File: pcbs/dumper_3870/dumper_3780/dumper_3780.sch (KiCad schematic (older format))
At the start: 23 parts, among them J1 Conn_01x03_Female, U1 MK3870, U2 Pico, U3 LM317T, U4 4066, U5 LM317T

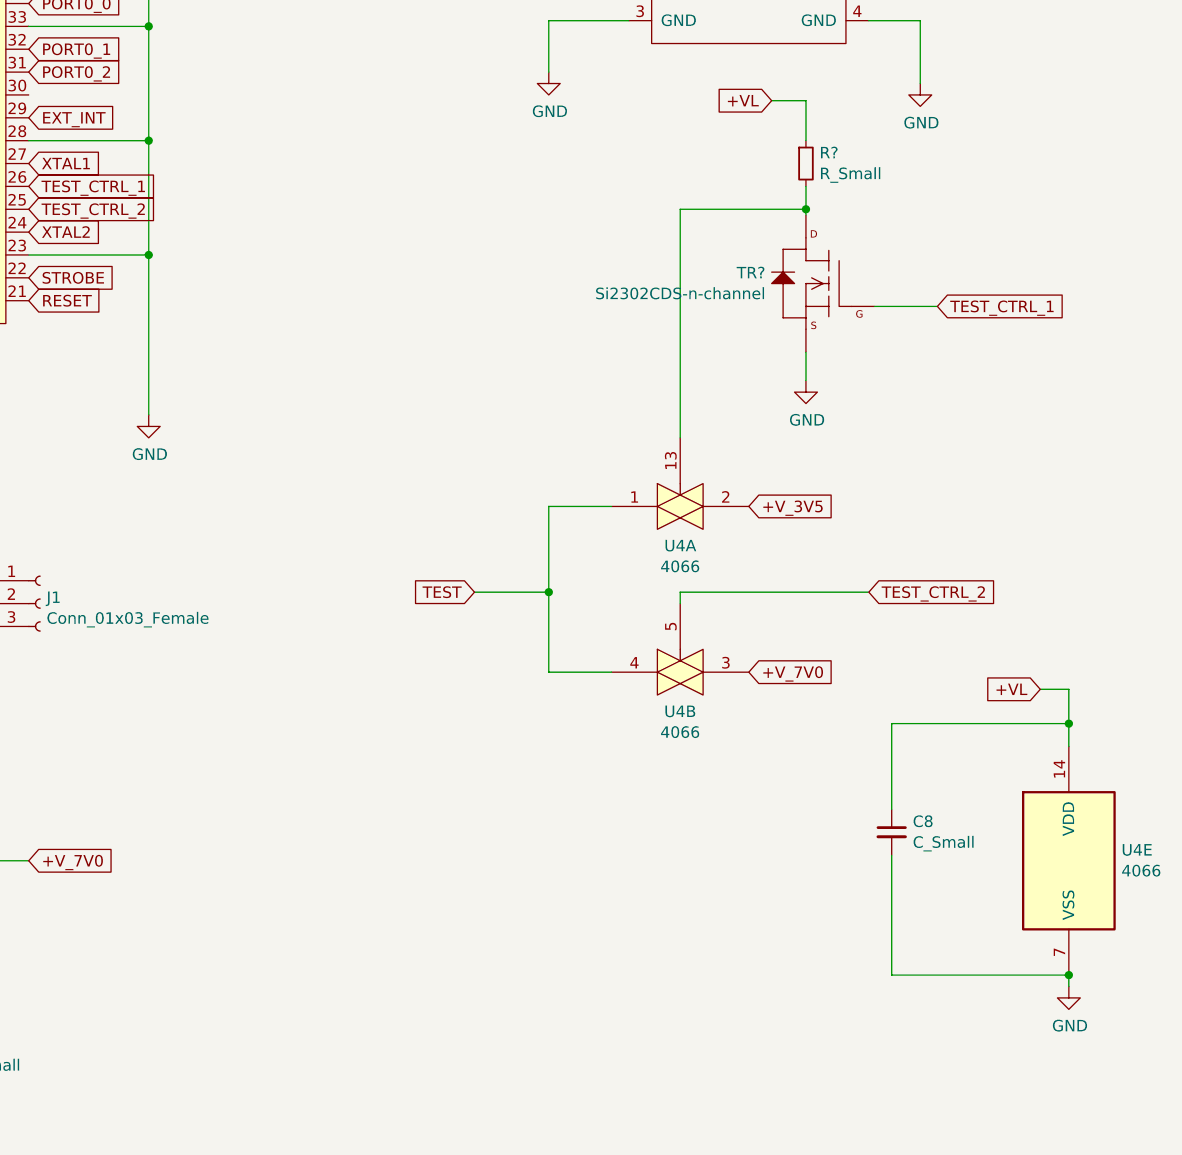
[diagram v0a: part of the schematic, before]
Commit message: Added PDF of V2.0 shematic which has level shifters added. No PCb of this yet.
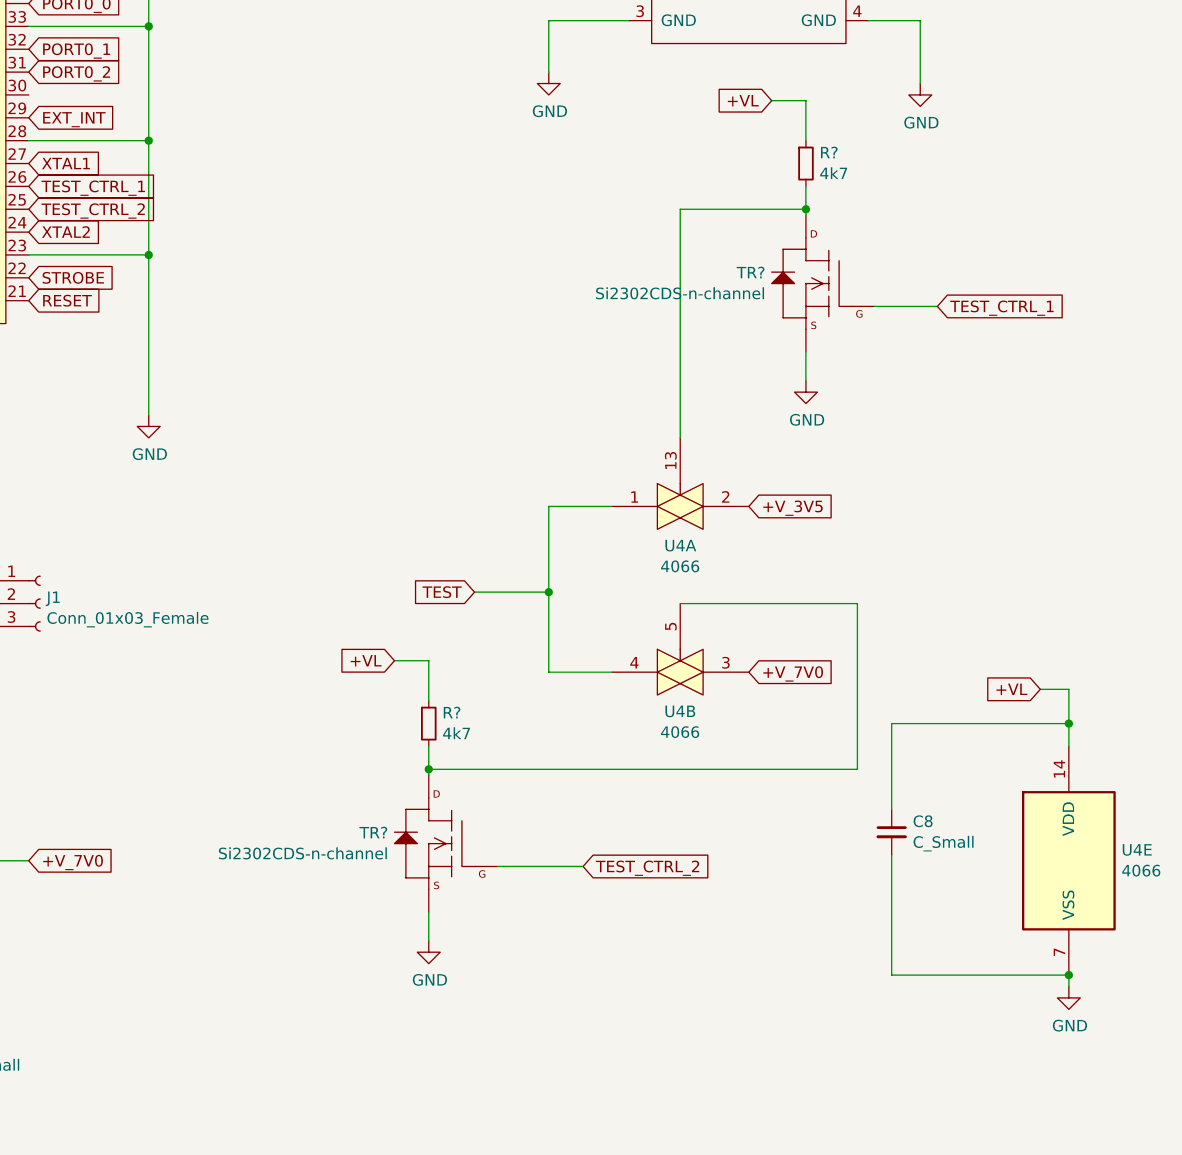
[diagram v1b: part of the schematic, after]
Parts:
- added R?: 4k7, symbol Device:R_Small
- added TR?: Si2302CDS-n-channel, Package_TO_SOT_SMD:SOT-23, symbol New_Library:Si2302CDS-n-channel
- R?: value R_Small -> 4k7
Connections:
- net +VL: now also R?.1
- net GND: now also TR?.2 (S)
- net TEST_CTRL_2: now also TR?.1 (G); no longer U4.5
- new net: R?.2, TR?.3 (D), U4.5
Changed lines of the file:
@@
 Sheet 1 1
 Title ""
-Date ""
-Rev ""
+Date "2024-02-18"
+Rev "2.0"
 Comp ""
-Comment1 ""
+Comment1 "Level shifters added"
 Comment2 ""
 Comment3 ""
@@
 Text GLabel 10025 3275 2    50   Input ~ 0
 TEST_CTRL_1
-Text GLabel 9725 4525 2    50   Input ~ 0
+Text GLabel 8475 5725 2    50   Input ~ 0
 TEST_CTRL_2
-Wire Wire Line
-	9725 4525 8900 4525
-Wire Wire Line
-	8900 4525 8900 4575
 Text GLabel 6050 2750 2    50   Input ~ 0
 TEST_CTRL_1
@@
 P 9450 2650
 F 0 "R?" H 9509 2696 50  0000 L CNN
-F 1 "R_Small" H 9509 2605 50  0000 L CNN
+F 1 "4k7" H 9509 2605 50  0000 L CNN
 F 2 "" H 9450 2650 50  0001 C CNN
 F 3 "~" H 9450 2650 50  0001 C CNN
@@
 Wire Wire Line
 	9750 3275 10025 3275
+$Comp
+L Device:R_Small R?
+U 1 1 65D24B8F
+P 7800 5100
+F 0 "R?" H 7859 5146 50  0000 L CNN
+F 1 "4k7" H 7859 5055 50  0000 L CNN
+F 2 "" H 7800 5100 50  0001 C CNN
+F 3 "~" H 7800 5100 50  0001 C CNN
+	1    7800 5100
+	1    0    0    -1
+$EndComp
+$Comp
+L New_Library:Si2302CDS-n-channel TR?
+U 1 1 65D24B95
+P 7900 5625
+F 0 "TR?" H 8177 5671 50  0000 L CNN
+F 1 "Si2302CDS-n-channel" H 8177 5580 50  0000 L CNN
+F 2 "Package_TO_SOT_SMD:SOT-23" H 7930 5775 20  0001 C CNN
+F 3 "" H 7900 5625 50  0001 C CNN
+	1    7900 5625
+	-1   0    0    -1
+$EndComp
+Text GLabel 7650 4825 0    50   Input ~ 0
++VL
+Wire Wire Line
+	7650 4825 7800 4825
+Wire Wire Line
+	7800 4825 7800 5000
+$Comp
+L power:GND #PWR?
+U 1 1 65D24BA3
+P 7800 6050
+F 0 "#PWR?" H 7800 5800 50  0001 C CNN
+F 1 "GND" H 7805 5877 50  0000 C CNN
+F 2 "" H 7800 6050 50  0001 C CNN
+F 3 "" H 7800 6050 50  0001 C CNN
+	1    7800 6050
+	1    0    0    -1
+$EndComp
+Wire Wire Line
+	7800 5925 7800 6050
+Wire Wire Line
+	7800 5200 7800 5300
+Wire Wire Line
+	8475 5725 8100 5725
+Wire Wire Line
+	7800 5300 9675 5300
+Wire Wire Line
+	9675 5300 9675 4575
+Wire Wire Line
+	9675 4575 8900 4575
+Connection ~ 7800 5300
+Wire Wire Line
+	7800 5300 7800 5325
 $EndSCHEMATC
